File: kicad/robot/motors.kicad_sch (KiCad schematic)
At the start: 15 parts, among them J3 67996-412HLF, Q6 SN74AHC125RGYR, U8 DRV8830DRCR, U9 DRV8830DRCR

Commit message: WARNING more BOM batch edits
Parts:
- Q6: Part Number (none) -> SN74AHC125RGYR
- U8, U9: Part Number (none) -> DRV8830DRCR
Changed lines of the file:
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@@
       (effects (font (size 1.524 1.524)) hide)
+    )
+    (property "Part Number" "SN74AHC125RGYR" (id 4) (at 218.44 160.02 0)
+      (effects (font (size 1.27 1.27)) hide)
     )
     (pin "PAD")
@@
       (effects (font (size 1.27 1.27)) hide)
     )
+    (property "Part Number" "DRV8830DRCR" (id 10) (at 96.52 129.54 0)
+      (effects (font (size 1.27 1.27)) hide)
+    )
     (pin "1")
     (pin "10")
@@
       (effects (font (size 1.27 1.27)) hide)
     )
+    (property "Part Number" "DRV8830DRCR" (id 10) (at 96.52 58.42 0)
+      (effects (font (size 1.27 1.27)) hide)
+    )

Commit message: Added stock counts to parts I have
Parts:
- Q6: Stock (none) -> 50
- U8, U9: Stock (none) -> 30
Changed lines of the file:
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@@
+      (effects (font (size 1.27 1.27)) hide)
+    )
+    (property "Stock" "50" (id 5) (at 218.44 160.02 0)
       (effects (font (size 1.27 1.27)) hide)
     )
@@
       (effects (font (size 1.27 1.27)) hide)
     )
+    (property "Stock" "30" (id 11) (at 96.52 129.54 0)
+      (effects (font (size 1.27 1.27)) hide)
+    )
     (pin "1")
     (pin "10")
@@
       (effects (font (size 1.27 1.27)) hide)
     )
+    (property "Stock" "30" (id 11) (at 96.52 58.42 0)
+      (effects (font (size 1.27 1.27)) hide)
+    )

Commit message: Batch BOM edits adding manufactuer and part numbers only
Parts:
- Q6: Manufacturer (none) -> Texas Instruments
- R28, R31: Manufacturer (none) -> Stackpole Electronics; Part Number (none) -> RMCF0603JT10K0
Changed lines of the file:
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@@
+      (effects (font (size 1.27 1.27)) hide)
+    )
+    (property "Manufacturer" "Texas Instruments" (id 6) (at 218.44 160.02 0)
       (effects (font (size 1.27 1.27)) hide)
     )
@@
       (effects (font (size 1.27 1.27)) hide)
     )
+    (property "Manufacturer" "Stackpole Electronics" (id 4) (at 67.31 41.91 0)
+      (effects (font (size 1.27 1.27)) hide)
+    )
+    (property "Part Number" "RMCF0603JT10K0" (id 5) (at 67.31 41.91 0)
+      (effects (font (size 1.27 1.27)) hide)
+    )
     (pin "1")
     (pin "2")
@@
       (effects (font (size 1.27 1.27)) hide)
     )
+    (property "Manufacturer" "Stackpole Electronics" (id 4) (at 73.66 111.76 0)
+      (effects (font (size 1.27 1.27)) hide)
+    )
+    (property "Part Number" "RMCF0603JT10K0" (id 5) (at 73.66 111.76 0)
+      (effects (font (size 1.27 1.27)) hide)
+    )

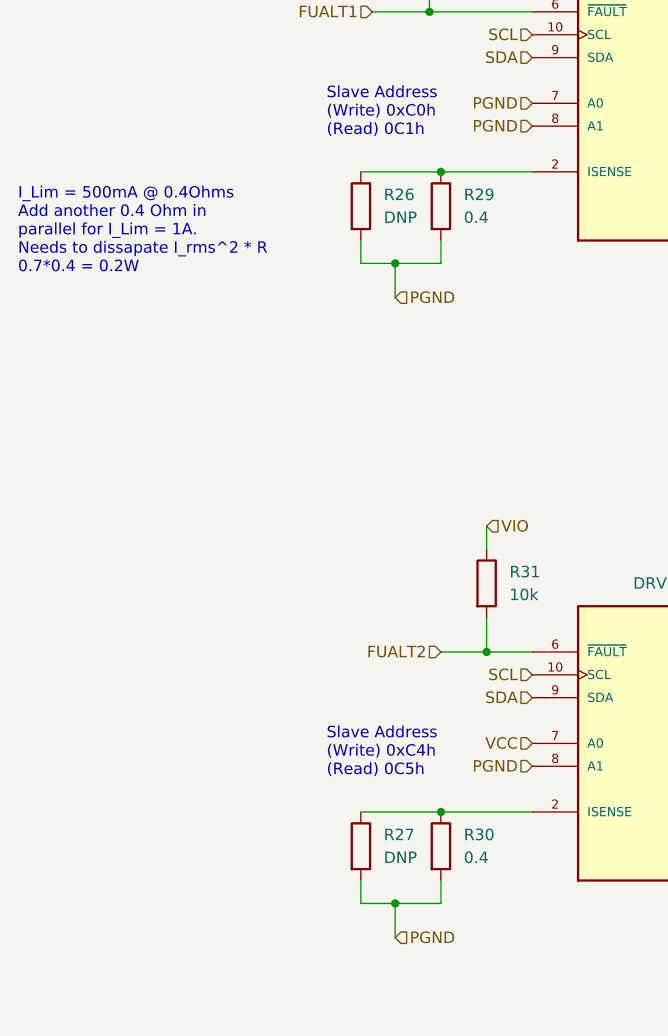
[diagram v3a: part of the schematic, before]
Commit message: Mainly just small value resistor tweaks and notes on their required power ratings.
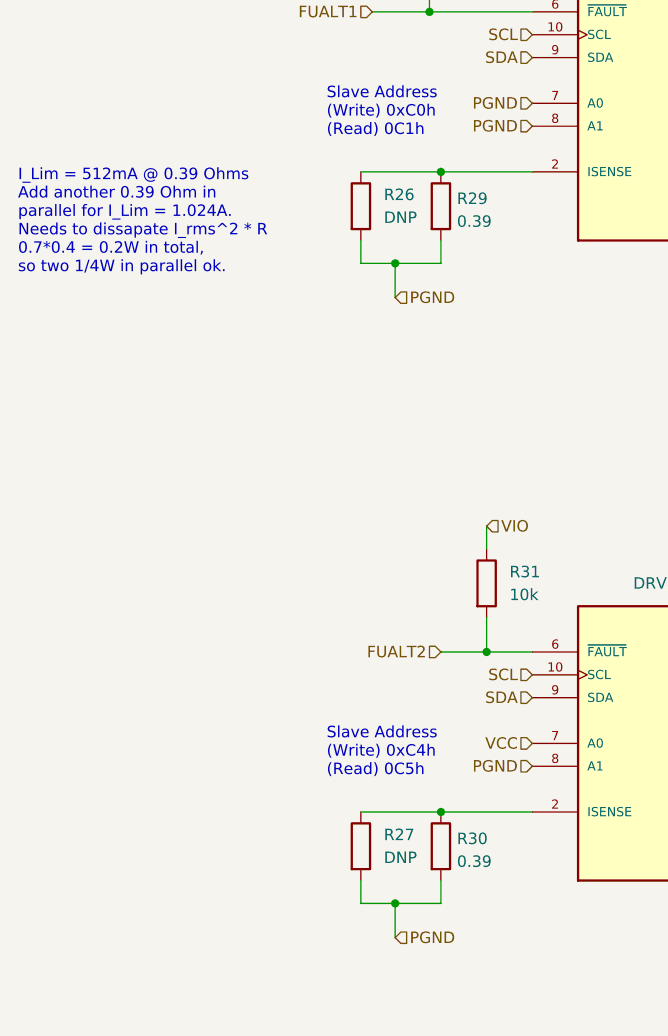
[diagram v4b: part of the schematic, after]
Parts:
- R29, R30: value 0.4 -> 0.39
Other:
- note added: "I_Lim = 512mA @ 0.39 Ohms Add another 0.39 Ohm in parallel for I_Lim = 1.024A. Needs to dissapate I_rms^2 * R 0.7*0.4 = 0.2W in total, so two 1/4W in parallel ok."
- note removed: "I_Lim = 500mA @ 0.4Ohms Add another 0.4 Ohm in parallel for I_Lim = 1A. Needs to dissapate I_rms^2 * R 0.7*0.4 = 0.2W"
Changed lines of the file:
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@@
     (effects (font (size 1.27 1.27)) (justify left bottom))
   )
-  (text "I_Lim = 500mA @ 0.4Ohms\nAdd another 0.4 Ohm in \nparallel for I_Lim = 1A.\nNeeds to dissapate I_rms^2 * R\n0.7*0.4 = 0.2W\n"
+  (text "I_Lim = 512mA @ 0.39 Ohms\nAdd another 0.39 Ohm in \nparallel for I_Lim = 1.024A.\nNeeds to dissapate I_rms^2 * R\n0.7*0.4 = 0.2W in total, \nso two 1/4W in parallel ok.\n"
     (at 21.59 77.47 0)
     (effects (font (size 1.27 1.27)) (justify left bottom))
@@
       (effects (font (size 1.27 1.27)) hide)
     )
+    (property "Description" "1/4W" (id 4) (at 59.69 140.97 0)
+      (effects (font (size 1.27 1.27)) hide)
+    )
     (pin "1")
     (pin "2")
@@
       (effects (font (size 1.27 1.27)) hide)
     )
+    (property "Description" "1/4W" (id 4) (at 59.69 69.85 0)
+      (effects (font (size 1.27 1.27)) hide)
+    )
     (pin "1")
     (pin "2")
@@
   (symbol (lib_id "Device:R") (at 68.58 140.97 0) (unit 1)
     (in_bom yes) (on_board yes) (fields_autoplaced)
-    (property "Reference" "R30" (id 0) (at 71.12 139.6999 0)
-      (effects (font (size 1.27 1.27)) (justify left))
-    )
-    (property "Value" "0.4" (id 1) (at 71.12 142.2399 0)
+    (property "Reference" "R30" (id 0) (at 70.358 140.1353 0)
+      (effects (font (size 1.27 1.27)) (justify left))
+    )
+    (property "Value" "0.39" (id 1) (at 70.358 142.6722 0)
       (effects (font (size 1.27 1.27)) (justify left))
     )
@@
     )
     (property "Datasheet" "~" (id 3) (at 68.58 140.97 0)
+      (effects (font (size 1.27 1.27)) hide)
+    )
+    (property "Description" "1/4W" (id 4) (at 68.58 140.97 0)
       (effects (font (size 1.27 1.27)) hide)
     )
@@
   (symbol (lib_id "Device:R") (at 68.58 69.85 0) (unit 1)
     (in_bom yes) (on_board yes) (fields_autoplaced)
-    (property "Reference" "R29" (id 0) (at 71.12 68.5799 0)
-      (effects (font (size 1.27 1.27)) (justify left))
-    )
-    (property "Value" "0.4" (id 1) (at 71.12 71.1199 0)
+    (property "Reference" "R29" (id 0) (at 70.358 69.0153 0)
+      (effects (font (size 1.27 1.27)) (justify left))
+    )
+    (property "Value" "0.39" (id 1) (at 70.358 71.5522 0)
       (effects (font (size 1.27 1.27)) (justify left))
     )
@@
       (effects (font (size 1.27 1.27)) hide)
     )
+    (property "Description" "1/4W" (id 4) (at 68.58 69.85 0)
+      (effects (font (size 1.27 1.27)) hide)
+    )

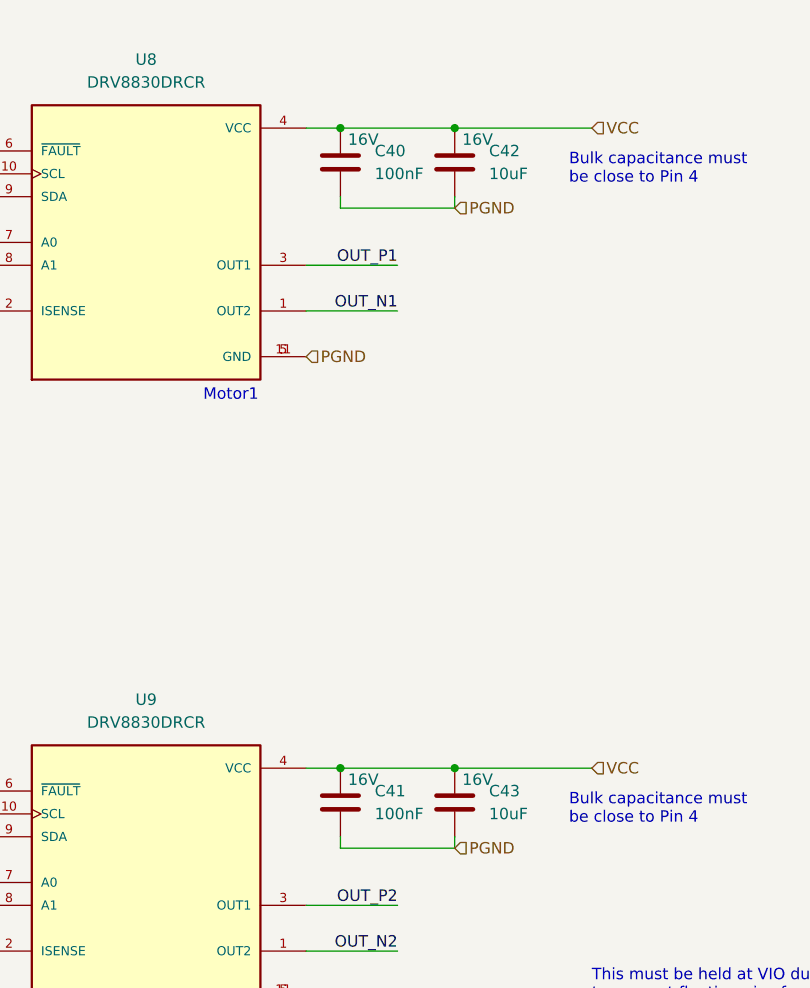
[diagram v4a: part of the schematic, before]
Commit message: bulk BOM edits. Mainly dealing with cap voltage ratings and part selection
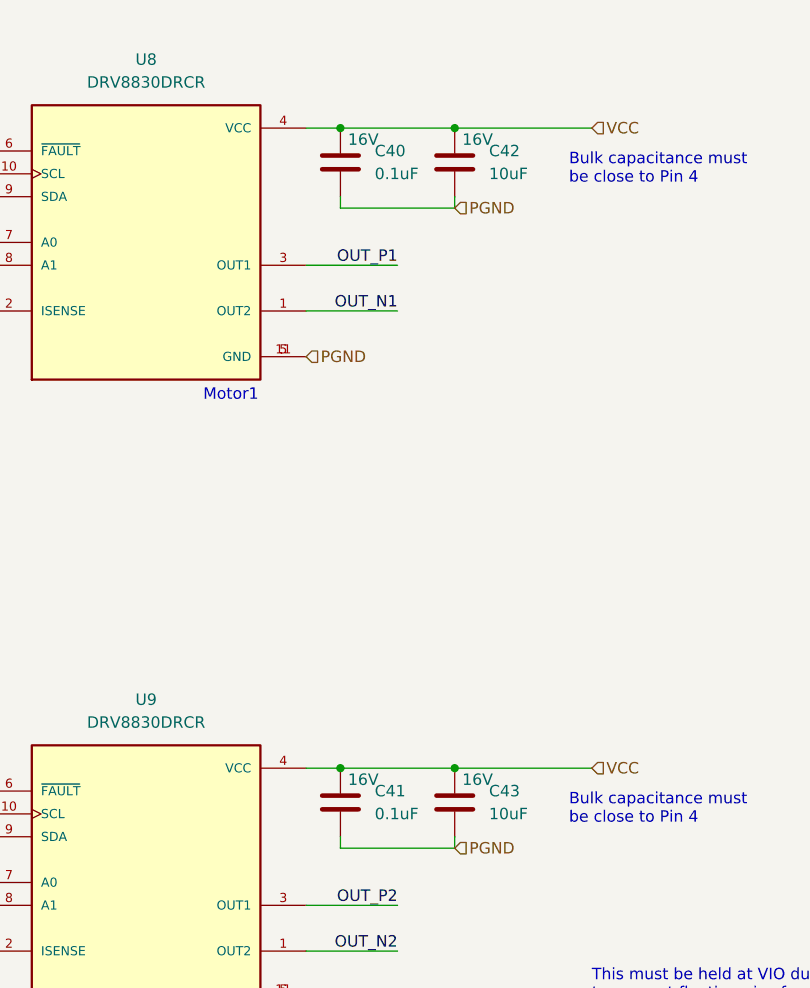
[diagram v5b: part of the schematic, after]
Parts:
- C40, C41: value 100nF -> 0.1uF; Manufacturer (none) -> Samsung; Part Number (none) -> CL21B104MACNNNC
- C42, C43: Manufacturer (none) -> Samsung; Part Number (none) -> CL21A106KOQNNNG
- C44: Manufacturer (none) -> Samsung; Part Number (none) -> CL10B104KB8NNWC
- R26, R27, R29, R30: Manufacturer (none) -> Panasonic; Part Number (none) -> ERJ-3RQJR39V
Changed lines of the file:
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@@
+      (effects (font (size 1.27 1.27)) hide)
+    )
+    (property "Manufacturer" "Panasonic" (id 5) (at 59.69 140.97 0)
+      (effects (font (size 1.27 1.27)) hide)
+    )
+    (property "Part Number" "ERJ-3RQJR39V" (id 6) (at 59.69 140.97 0)
       (effects (font (size 1.27 1.27)) hide)
     )
@@
     )
     (property "Description" "16V" (id 4) (at 133.35 46.99 0))
+    (property "Manufacturer" "Samsung" (id 5) (at 130.81 49.53 0)
+      (effects (font (size 1.27 1.27)) hide)
+    )
+    (property "Part Number" "CL21A106KOQNNNG" (id 6) (at 130.81 49.53 0)
+      (effects (font (size 1.27 1.27)) hide)
+    )
     (pin "1")
     (pin "2")
@@
       (effects (font (size 1.27 1.27)) (justify left))
     )
-    (property "Value" "100nF" (id 1) (at 121.92 50.7999 0)
+    (property "Value" "0.1uF" (id 1) (at 121.92 50.7999 0)
       (effects (font (size 1.27 1.27)) (justify left))
     )
@@
     )
     (property "Description" "16V" (id 4) (at 120.65 46.99 0))
+    (property "Manufacturer" "Samsung" (id 5) (at 118.11 49.53 0)
+      (effects (font (size 1.27 1.27)) hide)
+    )
+    (property "Part Number" "CL21B104MACNNNC" (id 6) (at 118.11 49.53 0)
+      (effects (font (size 1.27 1.27)) hide)
+    )
     (pin "1")
     (pin "2")
@@
       (effects (font (size 1.27 1.27)) hide)
     )
+    (property "Manufacturer" "Panasonic" (id 5) (at 59.69 69.85 0)
+      (effects (font (size 1.27 1.27)) hide)
+    )
+    (property "Part Number" "ERJ-3RQJR39V" (id 6) (at 59.69 69.85 0)
+      (effects (font (size 1.27 1.27)) hide)
+    )
     (pin "1")
     (pin "2")
@@
     )
     (property "Description" "1/4W" (id 4) (at 68.58 140.97 0)
+      (effects (font (size 1.27 1.27)) hide)
+    )
+    (property "Manufacturer" "Panasonic" (id 5) (at 68.58 140.97 0)
+      (effects (font (size 1.27 1.27)) hide)
+    )
+    (property "Part Number" "ERJ-3RQJR39V" (id 6) (at 68.58 140.97 0)
       (effects (font (size 1.27 1.27)) hide)
     )
@@
     )
     (property "Description" "16V" (id 4) (at 133.35 118.11 0))
+    (property "Manufacturer" "Samsung" (id 5) (at 130.81 120.65 0)
+      (effects (font (size 1.27 1.27)) hide)
+    )
+    (property "Part Number" "CL21A106KOQNNNG" (id 6) (at 130.81 120.65 0)
+      (effects (font (size 1.27 1.27)) hide)
+    )
     (pin "1")
     (pin "2")
@@
       (effects (font (size 1.27 1.27)) (justify left))
     )
-    (property "Value" "100nF" (id 1) (at 121.92 121.9199 0)
+    (property "Value" "0.1uF" (id 1) (at 121.92 121.9199 0)
       (effects (font (size 1.27 1.27)) (justify left))
     )
@@
     )
     (property "Description" "16V" (id 4) (at 120.65 118.11 0))
+    (property "Manufacturer" "Samsung" (id 5) (at 118.11 120.65 0)
+      (effects (font (size 1.27 1.27)) hide)
+    )
+    (property "Part Number" "CL21B104MACNNNC" (id 6) (at 118.11 120.65 0)
+      (effects (font (size 1.27 1.27)) hide)
+    )
     (pin "1")
     (pin "2")
@@
       (effects (font (size 1.27 1.27)) hide)
     )
+    (property "Manufacturer" "Samsung" (id 4) (at 251.46 161.29 0)
+      (effects (font (size 1.27 1.27)) hide)
+    )
+    (property "Part Number" "CL10B104KB8NNWC" (id 5) (at 251.46 161.29 0)
+      (effects (font (size 1.27 1.27)) hide)
+    )
     (pin "1")
     (pin "2")
@@
       (effects (font (size 1.27 1.27)) hide)
     )
+    (property "Manufacturer" "Panasonic" (id 5) (at 68.58 69.85 0)
+      (effects (font (size 1.27 1.27)) hide)
+    )
+    (property "Part Number" "ERJ-3RQJR39V" (id 6) (at 68.58 69.85 0)
+      (effects (font (size 1.27 1.27)) hide)
+    )
